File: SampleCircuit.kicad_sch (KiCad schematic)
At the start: 53 parts, among them J1 24V INPUT, J2 12V TEST, J3 5V TEST, J4 3.3V TEST, J5 SPEAKER, SW1 RESET, SW2 BOOT, U1 LMZM23601SILR, U15 TLV803S, U2 ESP32-S3-WROOM-1, U23 RV-3028-C7, U24 LMZM23601SILR, U25 LMZM23601SILR, U5 NS4168, U6 MicroSD

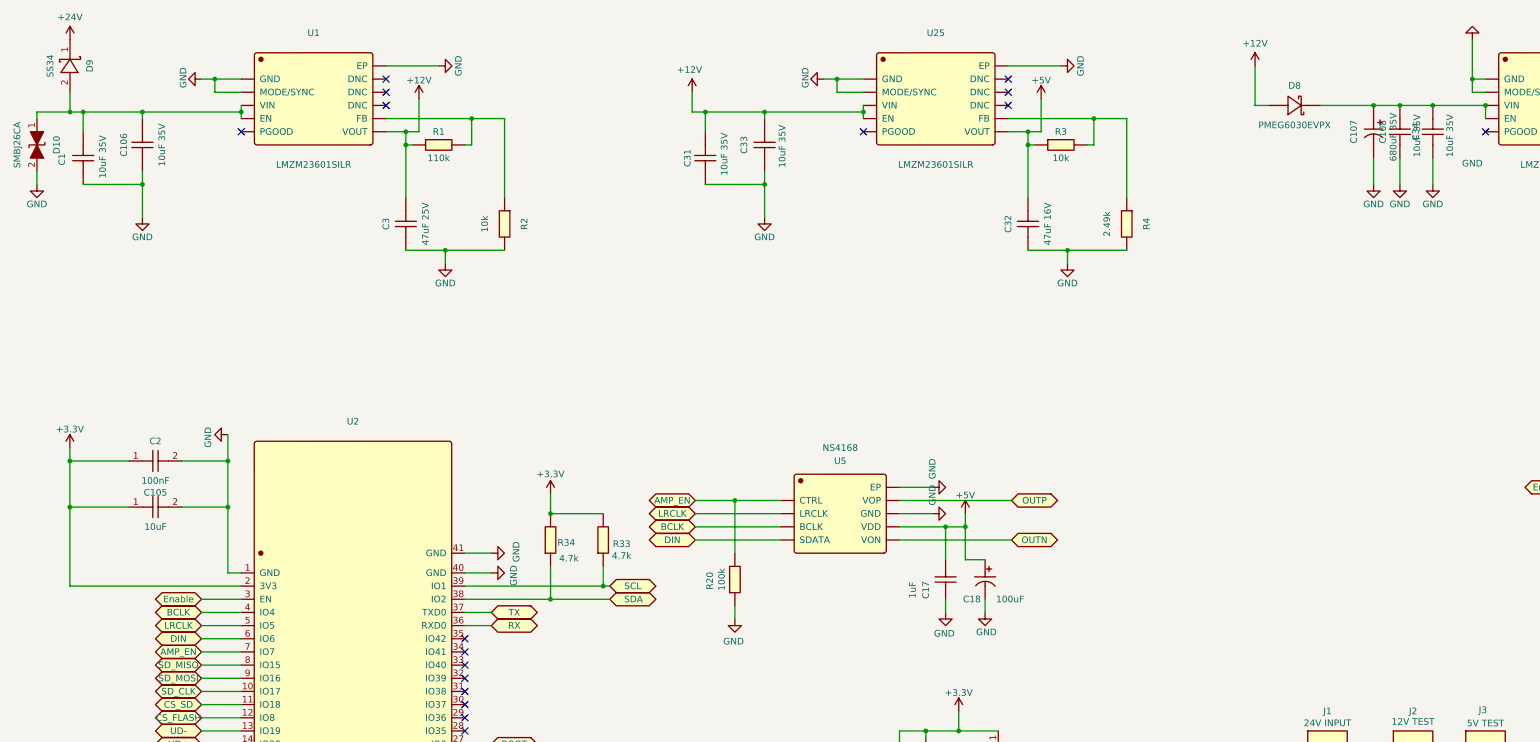
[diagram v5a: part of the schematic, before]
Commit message: Add PCB layout with functional block placement and antenna cutout
4"x4" board with ESP32-S3 antenna at bottom edge (180° rotation),
20x6mm PCB cutout underneath per Espressif specs. Components grouped
by schematic block: PSU chain across top (12V→5V→3.3V), connectors
at top edge, SD card at right edge, flash/RTC/audio grouped near
their bus connections. GND copper pour on both layers. 4x M6 mounting
holes inset 3/8" from edges. Includes JLCImport footprints, 3D models,
patches, and schematic/template updates.

Co-Authored-By: Claude Opus 4.6 <noreply@anthropic.com>
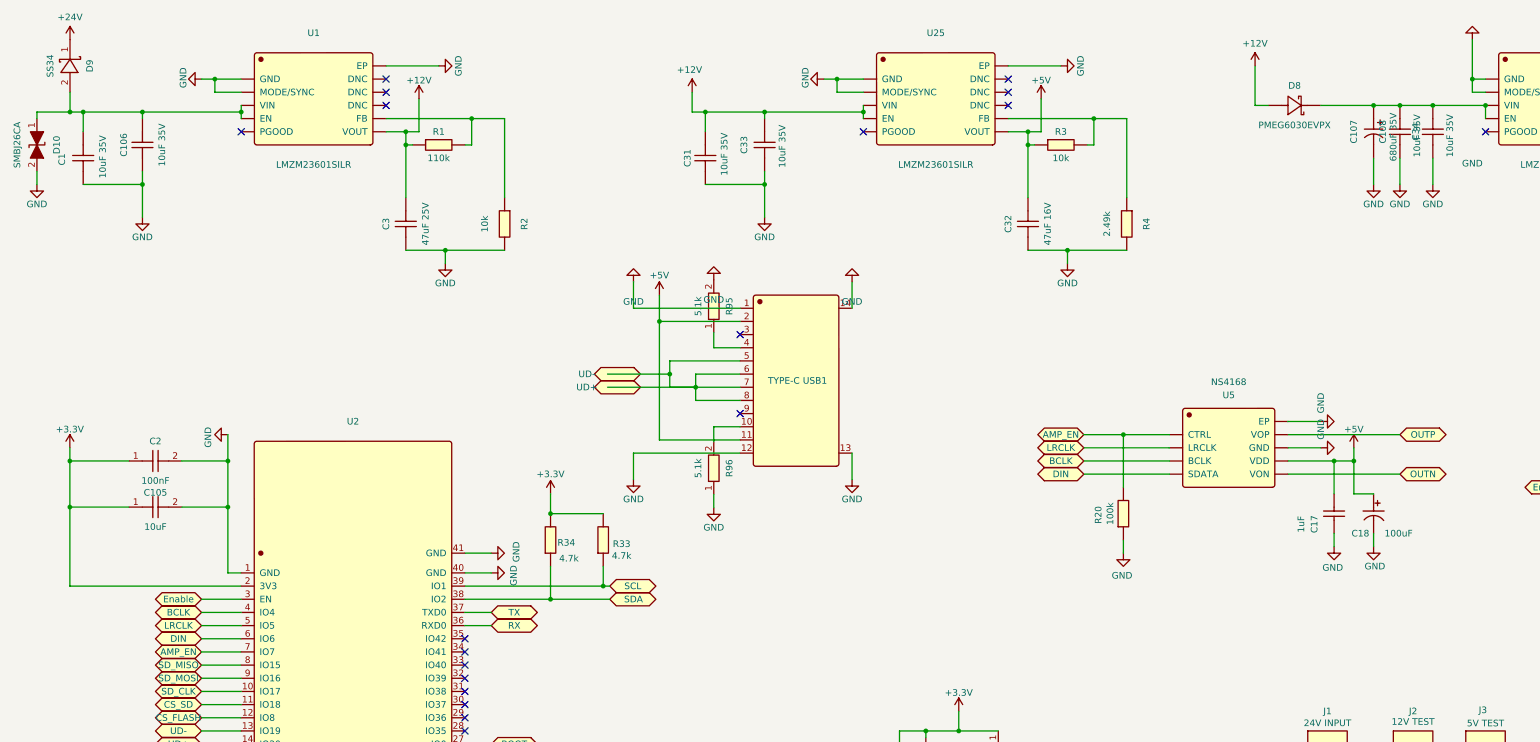
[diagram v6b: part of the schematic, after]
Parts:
- added R95, R96: 5.1k, JLCImport:0805W8F5101T5E, symbol JLCImport:0805W8F5101T5E
- added USB1: TYPE-C, JLCImport:TYPE-C_16PIN_2MD_073, symbol JLCImport:TYPE-C_16PIN_2MD_073
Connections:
- net +5V: now also USB1.11 (VBUS), USB1.2 (VBUS)
- net GND: now also R95.2, R96.1, USB1.1 (GND), USB1.12 (GND), USB1.13 (SHELL), USB1.14 (SHELL)
- new net: R96.2, USB1.10 (CC2)
- new net: R95.1, USB1.4 (CC1)
- new net: USB1.5 (DN2), USB1.6 (DP1), USB1.7 (DN1), USB1.8 (DP2)
- no-connect marks 40 -> 42
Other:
- moved on the sheet: C17, C18, R20, U5

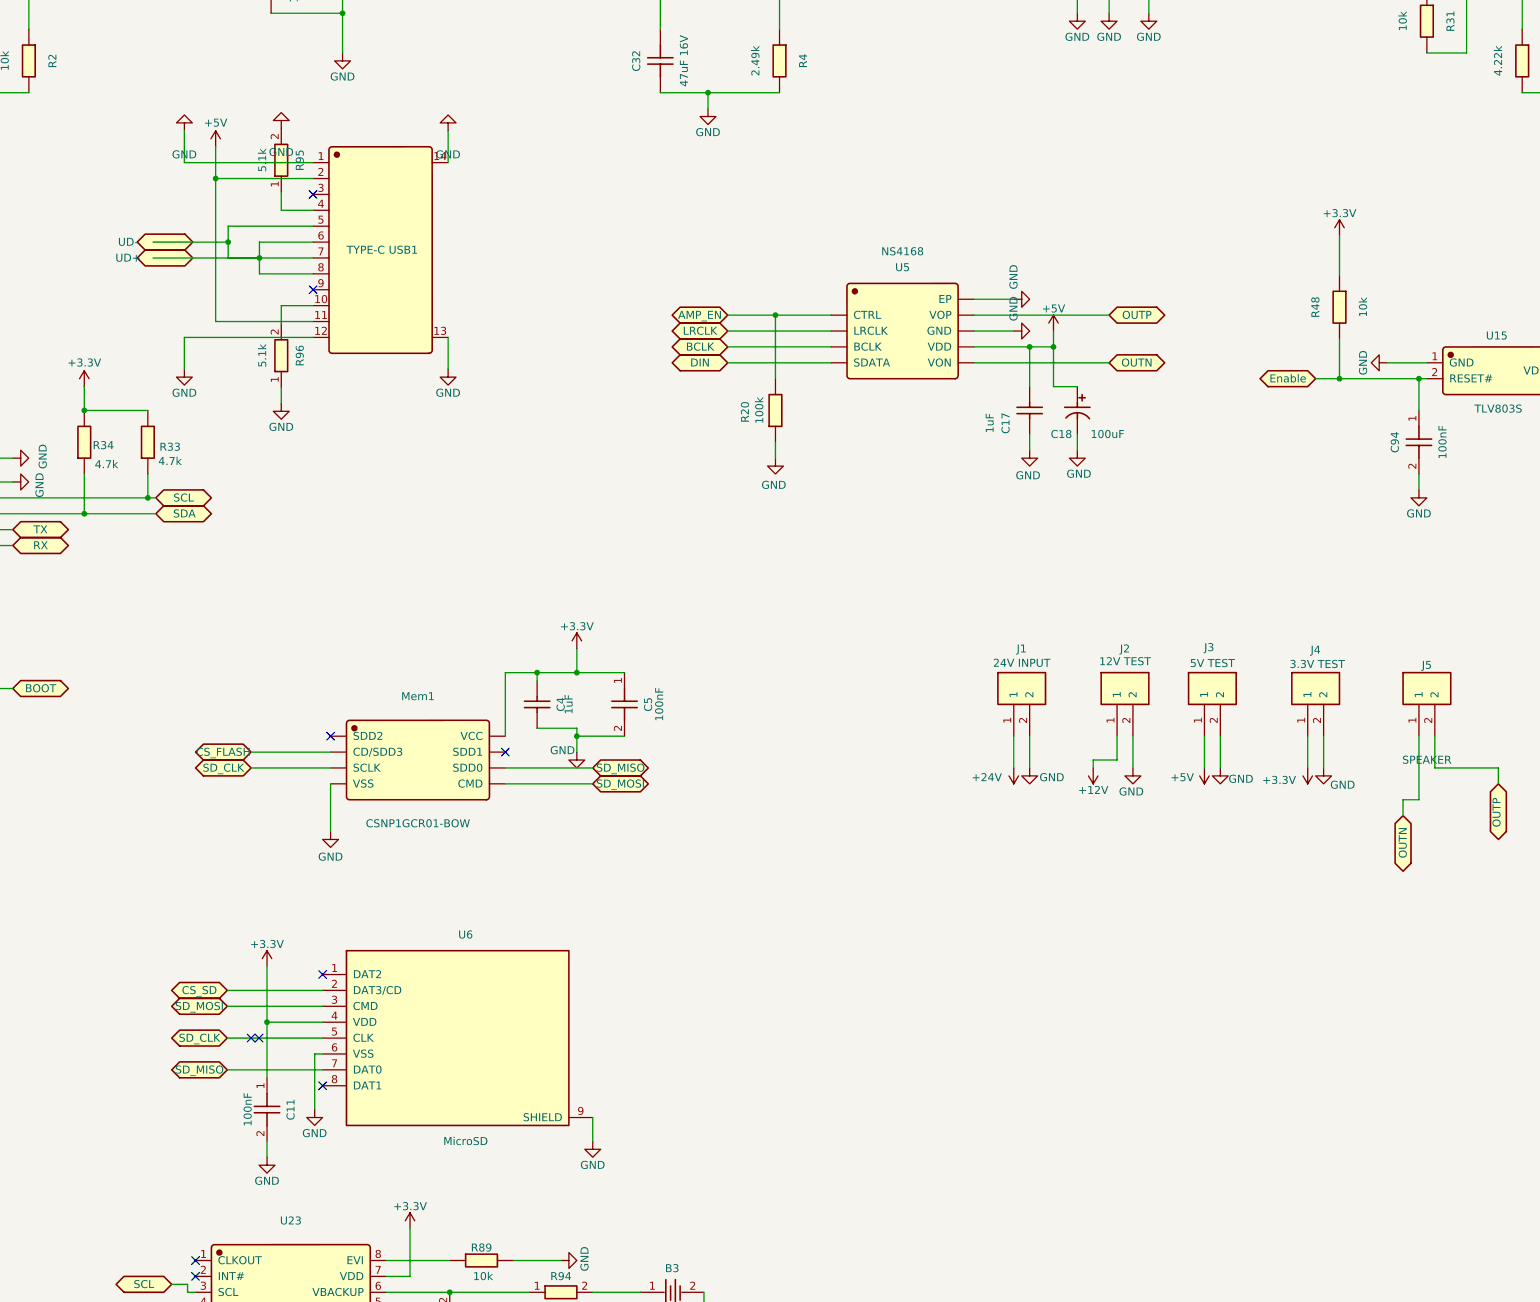
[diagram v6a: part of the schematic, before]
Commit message: Sync schematic, PCB, and new footprints for continuity on another system
Adds .gitignore, ERC report, new footprints (LED_0805_Green, LED0805-R-RD,
TF-SMD_TF-PUSH), DSN/SES routing files, and updates to schematic/PCB/symbols.

Co-Authored-By: Claude Opus 4.6 <noreply@anthropic.com>
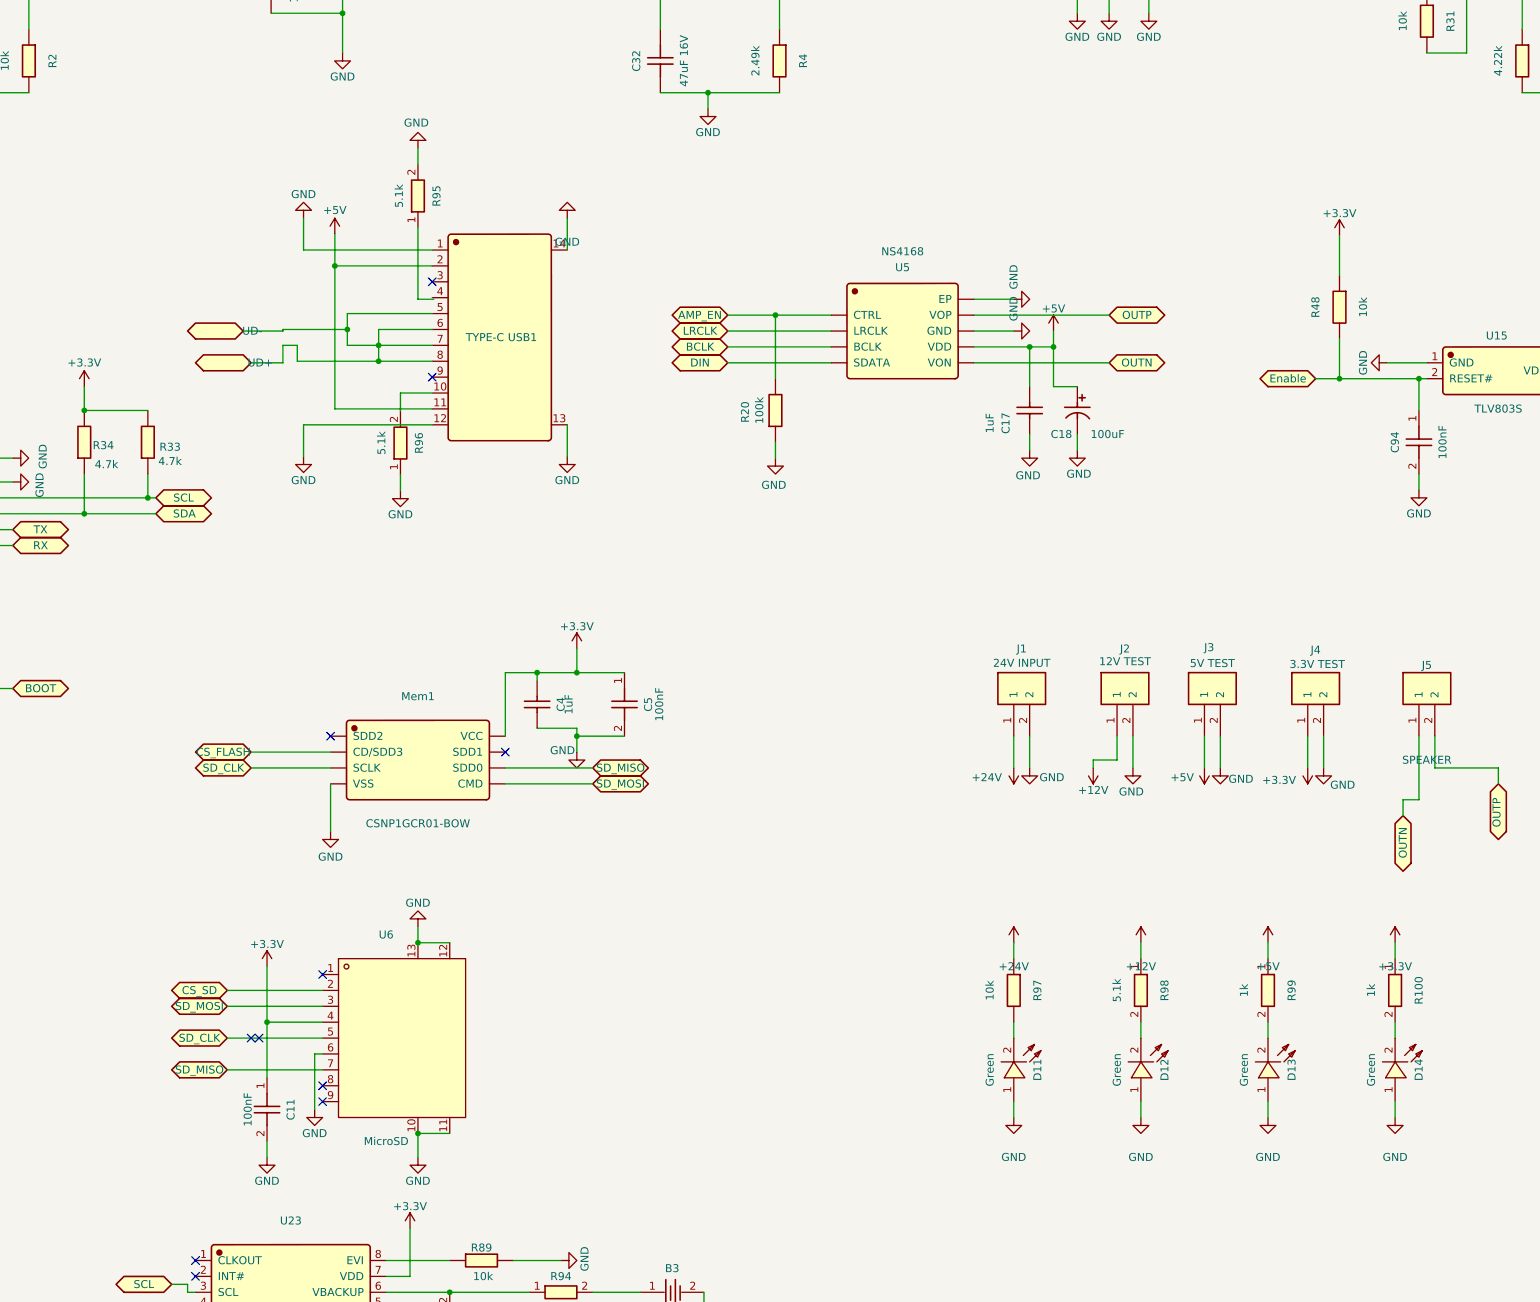
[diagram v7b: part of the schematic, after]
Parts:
- removed U6: MicroSD, JLCImport:Micro_SD_Card_C585354, symbol JLCImport:Micro_SD_Card_C585354
- added D11, D12, D13, D14: Green, JLCImport:LED0805-R-RD, symbol JLCImport:0805G(Green)
- added R100, R99: 1k, JLCImport:0805W8F1001T5E, symbol JLCImport:0805W8F1001T5E
- added R97: 10k, JLCImport:0805W8F1002T5E, symbol JLCImport:0805W8F1002T5E
- added R98: 5.1k, JLCImport:0805W8F5101T5E, symbol JLCImport:0805W8F5101T5E
- added U6: MicroSD, JLCImport:TF-SMD_TF-PUSH, symbol JLCImport:TFPUSH
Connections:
- net UD- is gone; now on net UD+: U2.13 (IO19)
- net +12V: now also R98.1
- net +24V: now also R97.1
- net +3.3V: now also R100.1, U6.4 (VDD)
- net +5V: now also R99.1
- net CS_SD: now also U6.2 (CD/DAT3)
- net GND: now also D11.1 (A), D12.1 (A), D13.1 (A), D14.1 (A), U6.10, U6.11, U6.12, U6.13, U6.6 (VSS)
- net SD_CLK: now also U6.5 (CLX)
- net SD_MISO: now also U6.7 (DAT0)
- net SD_MOSI: now also U6.3 (CMD)
- net UD+: now also USB1.5 (DN2), USB1.6 (DP1), USB1.7 (DN1), USB1.8 (DP2)
- net at USB1.4 (CC1): no longer R95.1
- new net: D11.2 (K), R97.2
- new net: D13.2 (K), R99.2
- new net: D14.2 (K), R100.2
- new net: D12.2 (K), R98.2
- no-connect marks 42 -> 43
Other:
- moved on the sheet: R95, R96, USB1

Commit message: Autoroute PCB with FreeRouting, fix GND zone thermals and edge clearance
- Swap discontinued 100k resistor C17407 to Basic C149504 (schematic + PCB)
- Set GND zone thermal relief to 0.5mm spoke/gap per spec
- Pull copper pour 1mm from board edge (was 0.3mm) per spec 18h
- Autoroute all nets via FreeRouting (2 manually completed near U23 RTC)
- DRC clean: 0 unconnected, 0 shorts, 3 non-critical warnings remaining

Co-Authored-By: Claude Opus 4.6 (1M context) <noreply@anthropic.com>
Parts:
- R20: LCSC C17407 -> C149504
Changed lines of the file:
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@@
 			)
 		)
-		(property "LCSC" "C17407"
+		(property "LCSC" "C149504"
 			(at 237.49 120.65 0)
 			(effects
